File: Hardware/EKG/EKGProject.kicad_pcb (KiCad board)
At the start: 2 copper layers, 94 x 81.5 mm, 66 parts, among them J1 Screw_Terminal_01x01, J10 Conn_01x04, J2 Screw_Terminal_01x01, J3 Screw_Terminal_01x01, J4 Conn_01x01, J5 Screw_Terminal_01x01, J6 Screw_Terminal_01x01, J7 Conn_01x01, J8 Conn_01x12, J9 Conn_01x16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

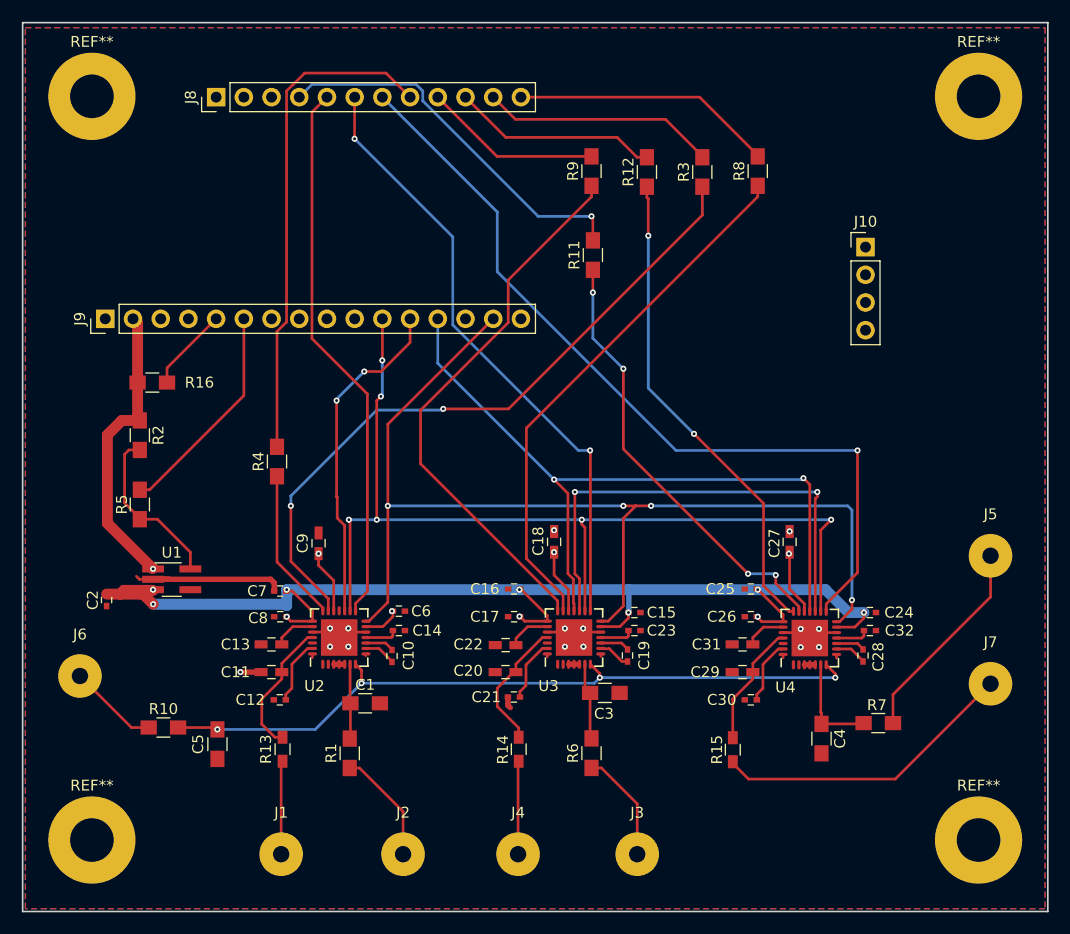
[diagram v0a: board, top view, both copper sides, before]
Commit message: add ground stiching
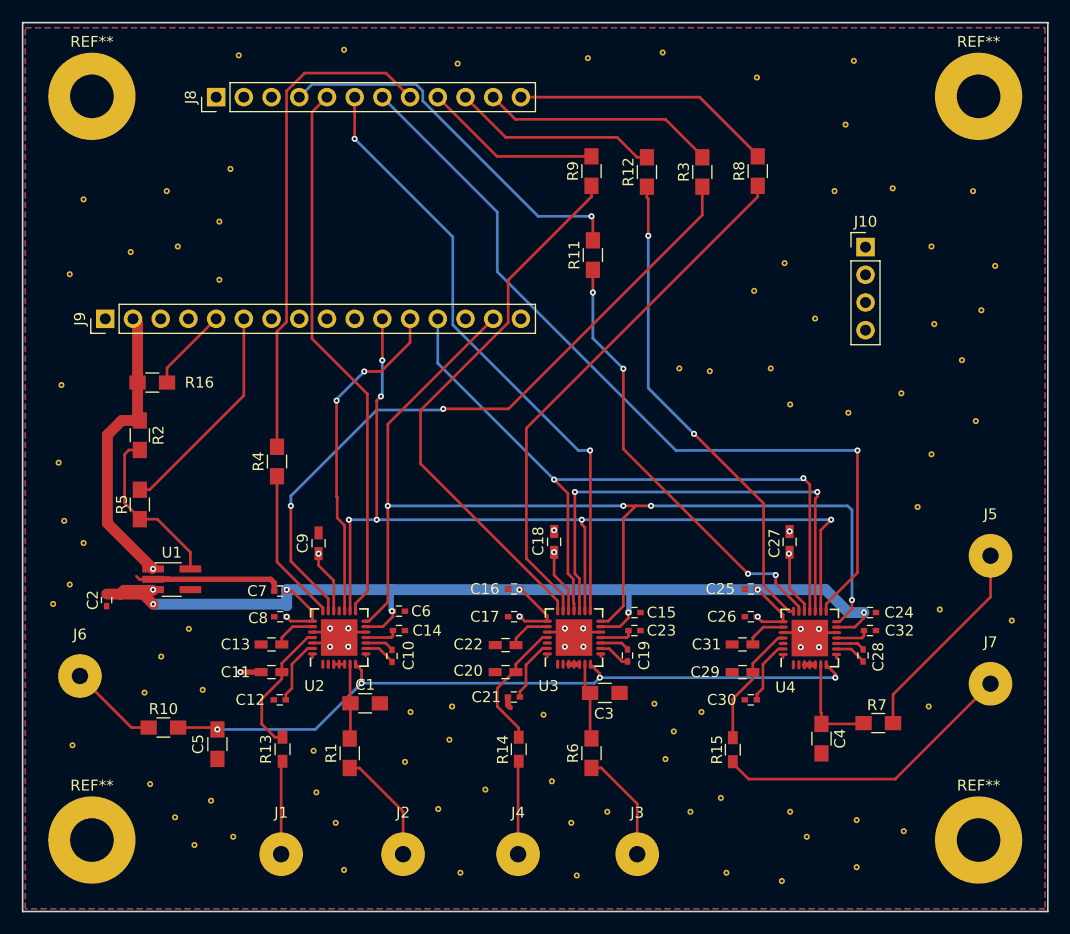
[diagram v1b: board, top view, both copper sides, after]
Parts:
- added REF**: GVIA, EKG:GVIA, F.Cu at (167.1, 128.0)
- added REF**: GVIA, EKG:GVIA, F.Cu at (201.3, 82.0)
- added REF**: GVIA, EKG:GVIA, F.Cu at (178.0, 133.6)
- added REF**: GVIA, EKG:GVIA, F.Cu at (175.7, 118.8)
- added REF**: GVIA, EKG:GVIA, F.Cu at (197.5, 109.4)
- added REF**: GVIA, EKG:GVIA, F.Cu at (204.1, 110.5)
- added REF**: GVIA, EKG:GVIA, F.Cu at (196.5, 118.3)
- added REF**: GVIA, EKG:GVIA, F.Cu at (174.7, 128.0)
- added REF**: GVIA, EKG:GVIA, F.Cu at (171.4, 118.1)
- added REF**: GVIA, EKG:GVIA, F.Cu at (194.2, 129.8)
- added REF**: GVIA, EKG:GVIA, F.Cu at (185.3, 130.3)
- added REF**: GVIA, EKG:GVIA, F.Cu at (164.3, 133.8)
- added REF**: GVIA, EKG:GVIA, F.Cu at (173.2, 120.6)
- added REF**: GVIA, EKG:GVIA, F.Cu at (189.9, 133.1)
- added REF**: GVIA, EKG:GVIA, F.Cu at (183.1, 134.3)
- added REF**: GVIA, EKG:GVIA, F.Cu at (189.9, 128.8)
- added REF**: GVIA, EKG:GVIA, F.Cu at (183.8, 128.0)
- added REF**: GVIA, EKG:GVIA, F.Cu at (130.0, 116.8)
- added REF**: GVIA, EKG:GVIA, F.Cu at (118.0, 121.9)
- added REF**: GVIA, EKG:GVIA, F.Cu at (127.4, 128.5)
- added REF**: GVIA, EKG:GVIA, F.Cu at (130.7, 127.0)
- added REF**: GVIA, EKG:GVIA, F.Cu at (132.8, 130.3)
- added REF**: GVIA, EKG:GVIA, F.Cu at (172.4, 123.2)
- added REF**: GVIA, EKG:GVIA, F.Cu at (119.0, 103.4)
- added REF**: GVIA, EKG:GVIA, F.Cu at (117.8, 107.2)
- added REF**: GVIA, EKG:GVIA, F.Cu at (129.2, 131.0)
- added REF**: GVIA, EKG:GVIA, F.Cu at (140.4, 126.2)
- added REF**: GVIA, EKG:GVIA, F.Cu at (151.6, 127.7)
- added REF**: GVIA, EKG:GVIA, F.Cu at (124.6, 117.1)
- added REF**: GVIA, EKG:GVIA, F.Cu at (128.7, 111.2)
- added REF**: GVIA, EKG:GVIA, F.Cu at (125.1, 125.5)
- added REF**: GVIA, EKG:GVIA, F.Cu at (142.2, 129.0)
- added REF**: GVIA, EKG:GVIA, F.Cu at (148.5, 123.4)
- added REF**: GVIA, EKG:GVIA, F.Cu at (200.6, 71.1)
- added REF**: GVIA, EKG:GVIA, F.Cu at (155.9, 126.0)
- added REF**: GVIA, EKG:GVIA, F.Cu at (142.9, 133.3)
- added REF**: GVIA, EKG:GVIA, F.Cu at (140.1, 122.4)
- added REF**: GVIA, EKG:GVIA, F.Cu at (149.0, 118.8)
- added REF**: GVIA, EKG:GVIA, F.Cu at (163.8, 129.0)
- added REF**: GVIA, EKG:GVIA, F.Cu at (126.2, 113.8)
- added REF**: GVIA, EKG:GVIA, F.Cu at (152.6, 121.4)
- added REF**: GVIA, EKG:GVIA, F.Cu at (152.8, 118.3)
- added REF**: GVIA, EKG:GVIA, F.Cu at (153.6, 133.6)
- added REF**: GVIA, EKG:GVIA, F.Cu at (119.0, 71.9)
- added REF**: GVIA, EKG:GVIA, F.Cu at (177.5, 126.7)
- added REF**: GVIA, EKG:GVIA, F.Cu at (131.5, 79.2)
- added REF**: GVIA, EKG:GVIA, F.Cu at (116.3, 108.9)
- added REF**: GVIA, EKG:GVIA, F.Cu at (117.3, 101.3)
- added REF**: GVIA, EKG:GVIA, F.Cu at (165.3, 58.9)
- added REF**: GVIA, EKG:GVIA, F.Cu at (116.8, 96.0)
- added REF**: GVIA, EKG:GVIA, F.Cu at (132.5, 69.1)
- added REF**: GVIA, EKG:GVIA, F.Cu at (123.4, 76.7)
- added REF**: GVIA, EKG:GVIA, F.Cu at (126.7, 71.1)
- added REF**: GVIA, EKG:GVIA, F.Cu at (172.1, 58.4)
- added REF**: GVIA, EKG:GVIA, F.Cu at (117.8, 78.7)
- added REF**: GVIA, EKG:GVIA, F.Cu at (161.2, 119.1)
- added REF**: GVIA, EKG:GVIA, F.Cu at (133.3, 58.6)
- added REF**: GVIA, EKG:GVIA, F.Cu at (189.7, 59.2)
- added REF**: GVIA, EKG:GVIA, F.Cu at (142.9, 58.1)
- added REF**: GVIA, EKG:GVIA, F.Cu at (186.1, 82.8)
- added REF**: GVIA, EKG:GVIA, F.Cu at (188.9, 65.0)
- added REF**: GVIA, EKG:GVIA, F.Cu at (153.3, 59.4)
- added REF**: GVIA, EKG:GVIA, F.Cu at (180.8, 60.7)
- added REF**: GVIA, EKG:GVIA, F.Cu at (162.0, 125.2)
- added REF**: GVIA, EKG:GVIA, F.Cu at (183.3, 77.7)
- added REF**: GVIA, EKG:GVIA, F.Cu at (187.9, 71.1)
- added REF**: GVIA, EKG:GVIA, F.Cu at (193.2, 70.8)
- added REF**: GVIA, EKG:GVIA, F.Cu at (117.0, 88.9)
- added REF**: GVIA, EKG:GVIA, F.Cu at (131.5, 73.9)
- added REF**: GVIA, EKG:GVIA, F.Cu at (202.6, 78.0)
- added REF**: GVIA, EKG:GVIA, F.Cu at (197.0, 83.3)
- added REF**: GVIA, EKG:GVIA, F.Cu at (196.8, 76.2)
- added REF**: GVIA, EKG:GVIA, F.Cu at (180.5, 80.2)
- added REF**: GVIA, EKG:GVIA, F.Cu at (189.2, 91.4)
- added REF**: GVIA, EKG:GVIA, F.Cu at (176.5, 87.6)
- added REF**: GVIA, EKG:GVIA, F.Cu at (183.8, 90.7)
- added REF**: GVIA, EKG:GVIA, F.Cu at (182.0, 87.4)
- added REF**: GVIA, EKG:GVIA, F.Cu at (173.7, 87.4)
- added REF**: GVIA, EKG:GVIA, F.Cu at (196.8, 95.2)
- added REF**: GVIA, EKG:GVIA, F.Cu at (195.5, 100.1)
- added REF**: GVIA, EKG:GVIA, F.Cu at (200.8, 92.2)
- added REF**: GVIA, EKG:GVIA, F.Cu at (199.6, 86.6)
- added REF**: GVIA, EKG:GVIA, F.Cu at (194.0, 89.6)
- added REF**: GVIA, EKG:GVIA, F.Cu at (127.7, 76.2)
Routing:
- net +1V8: track 107.5 -> 109.5 mm
- net Earth: track 33.0 -> 34.9 mm

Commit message: FINAL
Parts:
- added REF**: GVIA, EKG:GVIA, F.Cu at (172.3, 109.8)
- added REF**: GVIA, EKG:GVIA, F.Cu at (172.3, 111.5)
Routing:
- net +3V3: track 45.2 -> 104.2 mm
- net /MISO: track 67.3 -> 99.2 mm, vias 2 -> 3
- net /MOSI: track 75.1 -> 97.4 mm, vias 4 -> 6
- net Earth: track 34.9 -> 47.3 mm
- net +1V8: track 109.5 -> 110.8 mm
- net (no net): vias 0 -> 1
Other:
- rule trace_min: 0.0889 -> 0.0508
- rule via_min_drill: 0.3 -> 0.254
